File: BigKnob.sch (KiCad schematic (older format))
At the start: 10 parts, among them J1 NSJ12HF-1, J2 NSJ12HF-1, J3 NSJ12HF-1, J4 STEREO-JACK-SWITCHED-5-Pin, J5 STEREO-JACK-SWITCHED-5-Pin

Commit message: :punch: fixed schema
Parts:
- R1: renamed from R?; footprint (none) -> stahllabs:PTD904-1015F-A104
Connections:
- net CHASSIS_GND: now also R1.A3, R1.B3, R1.C3, R1.D3; no longer R1.A2, R1.B2, R1.C2, R1.D2
- net at J3.3 (RT): now also R1.B2; no longer R1.B3
- net at J3.5 (TT): now also R1.A2; no longer R1.A3
- net at J3.11 (TB): now also R1.C2; no longer R1.C3
- net at J3.9 (RB): now also R1.D2; no longer R1.D3
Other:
- moved on the sheet: J3A, J3B, R1A, R1B, R1C, R1D
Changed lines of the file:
@@
 $EndComp
 Wire Wire Line
-	3150 2700 3300 2700
-Wire Wire Line
-	3300 2700 3500 2700
-Wire Wire Line
-	3150 3600 3300 3600
-Wire Wire Line
-	3300 3600 3500 3600
-Wire Wire Line
-	3150 4750 3300 4750
-Wire Wire Line
-	3300 4750 3500 4750
+	3150 2700 3500 2700
+Wire Wire Line
+	3150 3600 3500 3600
+Wire Wire Line
+	3150 4750 3500 4750
 Text GLabel 3500 2700 2    60   Input ~ 0
 CHASSIS_GND
@@
 CHASSIS_GND
 Wire Wire Line
-	3150 5650 3300 5650
-Wire Wire Line
-	3300 5650 3500 5650
+	3150 5650 3500 5650
 Text GLabel 3500 5650 2    60   Input ~ 0
 CHASSIS_GND
@@
 L NSJ12HF-1 J3
 U 1 1 58E15C9F
-P 8350 3750
-F 0 "J3" H 8400 3350 60  0000 C CNN
-F 1 "NSJ12HF-1" H 8400 4050 60  0000 C CNN
-F 2 "stahllabs:NSJ12HF-1" H 8700 3900 60  0001 C CNN
-F 3 "http://www.neutrik.com/en/audio/plugs-and-jacks/stacking-jacks/nsj12hf-1" H 8400 3250 21  0001 C BIN
-	1    8350 3750
+P 8350 3700
+F 0 "J3" H 8400 3300 60  0000 C CNN
+F 1 "NSJ12HF-1" H 8400 4000 60  0000 C CNN
+F 2 "stahllabs:NSJ12HF-1" H 8700 3850 60  0001 C CNN
+F 3 "http://www.neutrik.com/en/audio/plugs-and-jacks/stacking-jacks/nsj12hf-1" H 8400 3200 21  0001 C BIN
+	1    8350 3700
 	-1   0    0    1
 $EndComp
@@
 L NSJ12HF-1 J3
 U 2 1 58E15D3A
-P 8350 4600
-F 0 "J3" H 8400 4200 60  0000 C CNN
-F 1 "NSJ12HF-1" H 8350 4900 60  0000 C CNN
-F 2 "stahllabs:NSJ12HF-1" H 8700 4750 60  0001 C CNN
-F 3 "http://www.neutrik.com/en/audio/plugs-and-jacks/stacking-jacks/nsj12hf-1" H 8400 4100 21  0001 C BIN
-	2    8350 4600
+P 8350 4700
+F 0 "J3" H 8400 4300 60  0000 C CNN
+F 1 "NSJ12HF-1" H 8350 5000 60  0000 C CNN
+F 2 "stahllabs:NSJ12HF-1" H 8700 4850 60  0001 C CNN
+F 3 "http://www.neutrik.com/en/audio/plugs-and-jacks/stacking-jacks/nsj12hf-1" H 8400 4200 21  0001 C BIN
+	2    8350 4700
 	-1   0    0    1
 $EndComp
 Wire Wire Line
-	7450 4050 7450 4500
-Wire Wire Line
-	7450 4500 7800 4500
-Wire Wire Line
-	7350 4300 7350 4650
-Wire Wire Line
-	7350 4650 7800 4650
+	6950 4250 6950 4600
+Wire Wire Line
+	6950 4600 7800 4600
+Wire Wire Line
+	6500 4750 7800 4750
 Wire Wire Line
 	3150 4550 4550 4550
 Wire Wire Line
-	4550 3600 4550 4550
-Wire Wire Line
-	4550 4550 4550 6500
-Wire Wire Line
-	6500 3550 7700 3550
-Wire Wire Line
-	7700 3550 7800 3650
-Text Notes 8950 3600 0    60   Italic 12
+	4550 3600 4550 6500
+Text Notes 8950 3550 0    60   Italic 12
 LEFT
 Text Notes 1800 2650 0    60   Italic 12
@@
 RIGHT
 Wire Wire Line
-	6500 3800 7800 3800
-Wire Wire Line
-	7550 4300 7800 4300
-Wire Wire Line
-	7550 3450 7550 3950
-Wire Wire Line
-	7550 3950 7550 4300
-Wire Wire Line
-	7550 4300 7550 4800
-Wire Wire Line
-	7800 3950 7550 3950
-Connection ~ 7550 3950
-Wire Wire Line
-	7550 4800 7800 4800
-Connection ~ 7550 4300
-Wire Wire Line
-	6500 4050 7450 4050
-Wire Wire Line
-	6500 4300 7350 4300
+	7650 4400 7800 4400
+Wire Wire Line
+	7650 3400 7650 4900
+Wire Wire Line
+	7800 3900 7650 3900
+Connection ~ 7650 3900
+Wire Wire Line
+	7650 4900 7800 4900
+Connection ~ 7650 4400
 Text Notes 8950 4450 0    60   Italic 12
 RIGHT
 Wire Wire Line
-	3150 2500 4450 2500
-Wire Wire Line
-	4450 2500 5000 2500
+	3150 2500 5000 2500
 Wire Wire Line
 	5000 2500 5000 3500
@@
 Connection ~ 3300 3600
 Wire Wire Line
-	7550 3450 7800 3450
-Text GLabel 7550 3450 0    60   Input ~ 0
-CHASSIS_GND
-Wire Wire Line
-	3150 3400 4550 3400
-Wire Wire Line
-	4550 3400 4800 3400
+	7650 3400 7800 3400
+Text GLabel 7650 3400 0    60   Input ~ 0
+CHASSIS_GND
+Wire Wire Line
+	3150 3400 4800 3400
 Wire Wire Line
 	4800 3400 4800 4000
@@
 	4800 4000 5000 4000
 Wire Wire Line
-	3150 5450 4450 5450
-Wire Wire Line
-	4450 5450 4800 5450
+	3150 5450 4800 5450
 Wire Wire Line
 	4800 5450 4800 4100
@@
 INPUT A\nmini jack
 Wire Wire Line
-	5550 3550 6100 3550
-Wire Wire Line
-	5550 3800 6100 3800
-Wire Wire Line
-	5550 4050 6100 4050
-Wire Wire Line
-	5550 4300 6100 4300
-Wire Wire Line
-	6300 3350 6600 3350
-Wire Wire Line
-	6600 3350 6600 3600
-Wire Wire Line
-	6600 3600 6600 3850
-Wire Wire Line
-	6600 3850 6600 4100
-Wire Wire Line
-	6600 4100 6600 4500
-Text GLabel 6600 4500 0    60   Input ~ 0
-CHASSIS_GND
-Wire Wire Line
-	6300 3600 6600 3600
-Connection ~ 6600 3600
-Wire Wire Line
-	6300 3850 6600 3850
-Wire Wire Line
-	6600 3850 6600 3850
-Connection ~ 6600 3850
-Wire Wire Line
-	6300 4100 6600 4100
-Connection ~ 6600 4100
-$Comp
-L PTD904-1015F-A104 R?
+	5550 4050 6300 4050
+Text GLabel 6100 5100 2    60   Input ~ 0
+CHASSIS_GND
+$Comp
+L PTD904-1015F-A104 R1
 U 1 1 58FEAB86
-P 6300 3550
-F 0 "R?" H 6300 3800 20  0000 C CNN
-F 1 "PTD904-1015F-A104" H 6300 3475 20  0000 C CNN
-F 2 "" H 6300 3550 60  0001 C CNN
-F 3 "" H 6300 3550 60  0001 C CNN
-	1    6300 3550
-	1    0    0    -1
-$EndComp
-$Comp
-L PTD904-1015F-A104 R?
+P 6300 3250
+F 0 "R1" H 6300 3500 20  0000 C CNN
+F 1 "PTD904-1015F-A104" H 6300 3175 20  0000 C CNN
+F 2 "stahllabs:PTD904-1015F-A104" H 6300 3250 60  0001 C CNN
+F 3 "" H 6300 3250 60  0001 C CNN
+	1    6300 3250
+	0    1    1    0
+$EndComp
+$Comp
+L PTD904-1015F-A104 R1
 U 2 1 58FEABBF
-P 6300 3800
-F 0 "R?" H 6300 4050 20  0000 C CNN
-F 1 "PTD904-1015F-A104" H 6300 3725 20  0000 C CNN
-F 2 "" H 6300 3800 60  0001 C CNN
-F 3 "" H 6300 3800 60  0001 C CNN
-	2    6300 3800
-	1    0    0    -1
-$EndComp
-$Comp
-L PTD904-1015F-A104 R?
-U 3 1 58FEAC45
-P 6300 4050
-F 0 "R?" H 6300 4300 20  0000 C CNN
-F 1 "PTD904-1015F-A104" H 6300 3975 20  0000 C CNN
-F 2 "" H 6300 4050 60  0001 C CNN
-F 3 "" H 6300 4050 60  0001 C CNN
-	3    6300 4050
-	1    0    0    -1
-$EndComp
-$Comp
-L PTD904-1015F-A104 R?
+P 6300 3750
+F 0 "R1" H 6300 4000 20  0000 C CNN
+F 1 "PTD904-1015F-A104" H 6300 3675 20  0000 C CNN
+F 2 "stahllabs:PTD904-1015F-A104" H 6300 3750 60  0001 C CNN
+F 3 "" H 6300 3750 60  0001 C CNN
+	2    6300 3750
+	0    1    1    0
+$EndComp
+$Comp
+L PTD904-1015F-A104 R1
 U 4 1 58FEAC80
-P 6300 4300
-F 0 "R?" H 6300 4550 20  0000 C CNN
-F 1 "PTD904-1015F-A104" H 6300 4225 20  0000 C CNN
-F 2 "" H 6300 4300 60  0001 C CNN
-F 3 "" H 6300 4300 60  0001 C CNN
-	4    6300 4300
-	1    0    0    -1
+P 6300 4750
+F 0 "R1" H 6300 5000 20  0000 C CNN
+F 1 "PTD904-1015F-A104" H 6300 4675 20  0000 C CNN
+F 2 "stahllabs:PTD904-1015F-A104" H 6300 4750 60  0001 C CNN
+F 3 "" H 6300 4750 60  0001 C CNN
+	4    6300 4750
+	0    1    1    0
 $EndComp
 Wire Notes Line
@@
 SWITCH
 Wire Notes Line
-	5900 4600 6700 4600
-Wire Notes Line
-	6700 4600 6700 3100
-Wire Notes Line
-	6700 3100 5900 3100
-Wire Notes Line
-	5900 3100 5900 4600
-Text Notes 6000 3250 0    99   Italic 20
+	5900 2700 6800 2700
+Wire Notes Line
+	5900 2700 5900 5250
+Text Notes 6000 2900 0    99   Italic 20
 VOLUME
+Wire Wire Line
+	6600 3250 6600 3600
+Wire Wire Line
+	6600 3600 7800 3600
+Wire Wire Line
+	6500 3750 7800 3750
+$Comp
+L PTD904-1015F-A104 R1
+U 3 1 58FEAC45
+P 6300 4250
+F 0 "R1" H 6300 4500 20  0000 C CNN
+F 1 "PTD904-1015F-A104" H 6300 4175 20  0000 C CNN
+F 2 "stahllabs:PTD904-1015F-A104" H 6300 4250 60  0001 C CNN
+F 3 "" H 6300 4250 60  0001 C CNN
+	3    6300 4250
+	0    1    1    0
+$EndComp
+Wire Wire Line
+	5550 3550 6000 3550
+Wire Wire Line
+	6000 3550 6000 3050
+Wire Wire Line
+	6000 3050 6300 3050
+Wire Wire Line
+	6500 3250 6600 3250
+Wire Wire Line
+	5550 4300 6200 4300
+Wire Wire Line
+	6200 4300 6200 4550
+Wire Wire Line
+	6200 4550 6300 4550
+Wire Wire Line
+	5550 3800 6200 3800
+Wire Wire Line
+	6200 3800 6200 3550
+Wire Wire Line
+	6200 3550 6300 3550
+Wire Notes Line
+	6800 2700 6800 5250
+Wire Wire Line
+	7450 3750 7450 3750
+Wire Wire Line
+	6950 4250 6500 4250
+Wire Wire Line
+	6100 3450 6100 5100
+Wire Wire Line
+	6100 3450 6300 3450
+Wire Wire Line
+	6300 3950 6100 3950
+Connection ~ 6100 3950
+Wire Wire Line
+	6300 4450 6100 4450
+Connection ~ 6100 4450
+Wire Wire Line
+	6300 4950 6100 4950
+Connection ~ 6100 4950
+Wire Notes Line
+	6800 5250 5900 5250
 $EndSCHEMATC

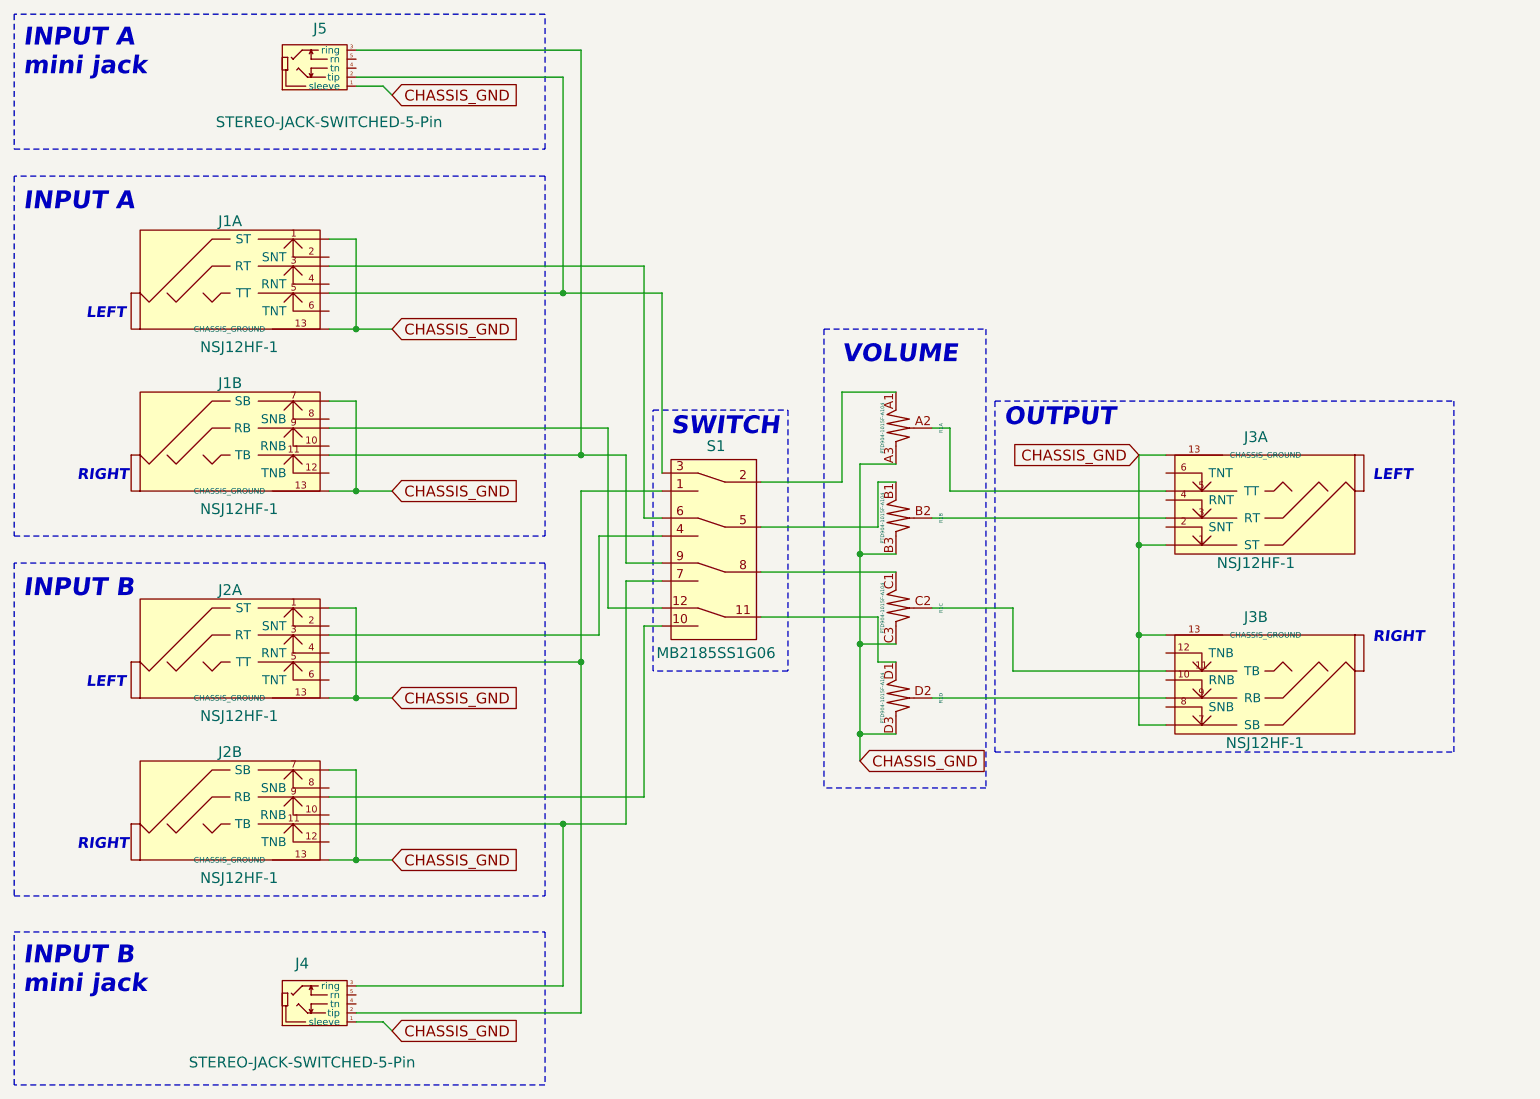
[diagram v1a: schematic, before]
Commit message: fix library paths
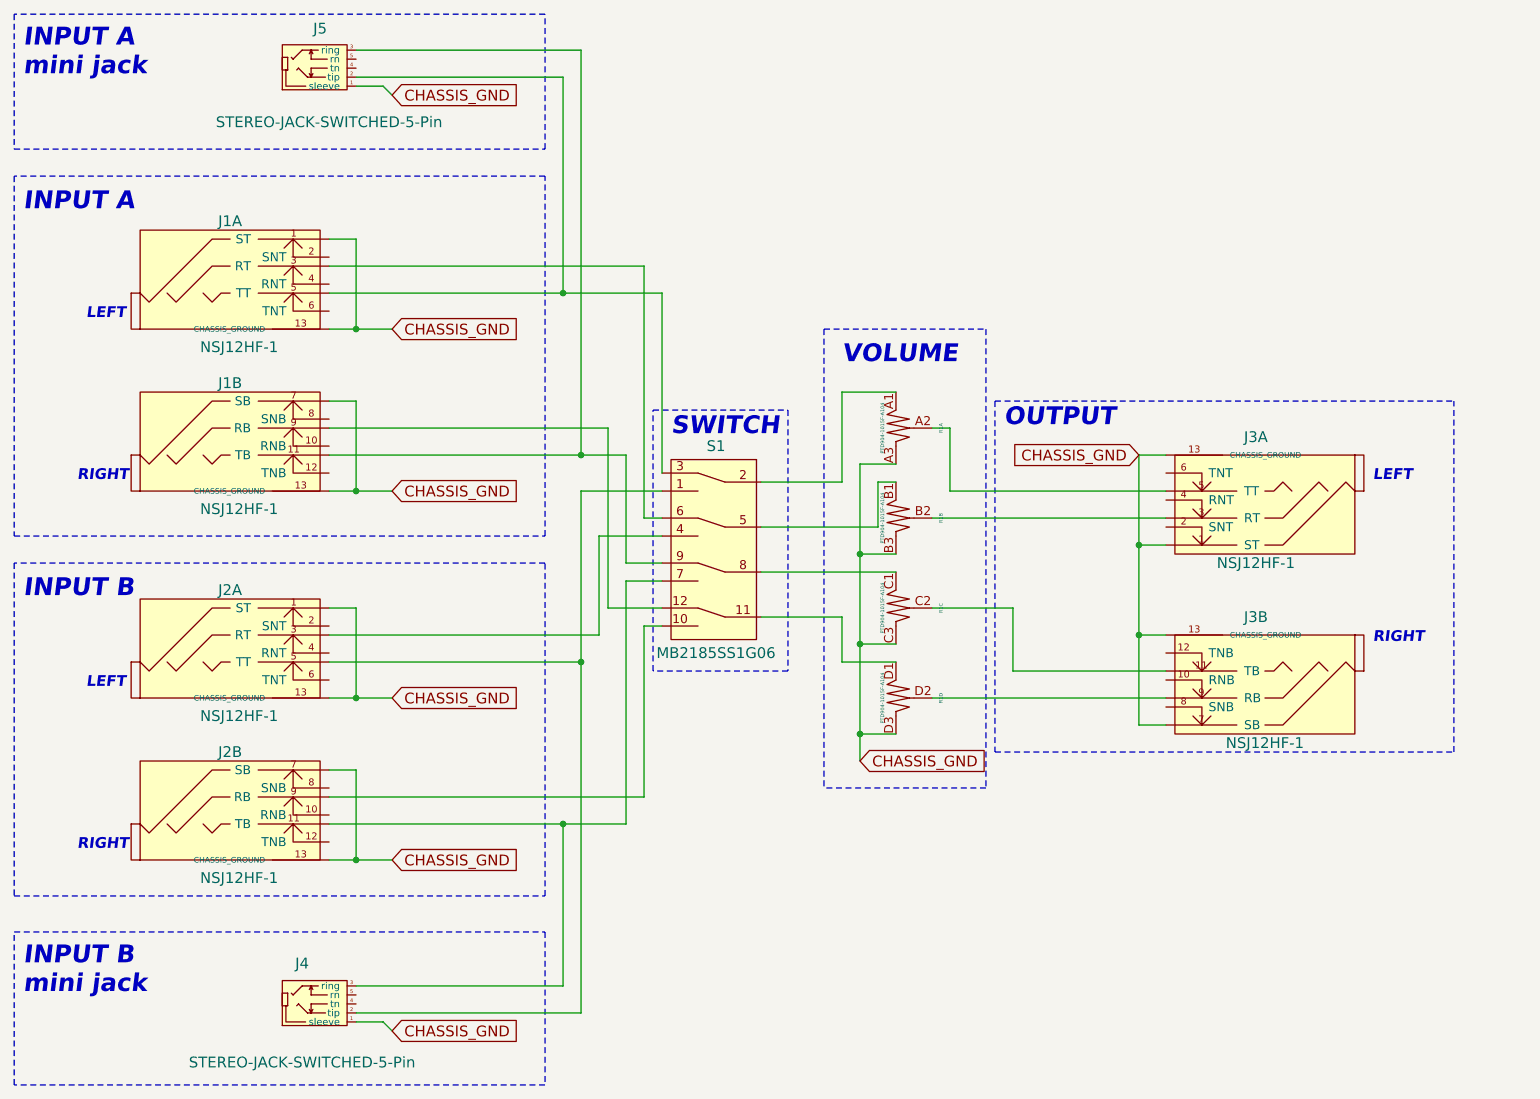
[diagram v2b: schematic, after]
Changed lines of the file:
@@
 $EndComp
 Wire Wire Line
-	3150 2700 3500 2700
-Wire Wire Line
-	3150 3600 3500 3600
-Wire Wire Line
-	3150 4750 3500 4750
+	3150 2700 3300 2700
+Wire Wire Line
+	3300 2700 3500 2700
+Wire Wire Line
+	3150 3600 3300 3600
+Wire Wire Line
+	3300 3600 3500 3600
+Wire Wire Line
+	3150 4750 3300 4750
+Wire Wire Line
+	3300 4750 3500 4750
 Text GLabel 3500 2700 2    60   Input ~ 0
 CHASSIS_GND
@@
 CHASSIS_GND
 Wire Wire Line
-	3150 5650 3500 5650
+	3150 5650 3300 5650
+Wire Wire Line
+	3300 5650 3500 5650
 Text GLabel 3500 5650 2    60   Input ~ 0
 CHASSIS_GND
@@
 	3150 4550 4550 4550
 Wire Wire Line
-	4550 3600 4550 6500
+	4550 3600 4550 4550
+Wire Wire Line
+	4550 4550 4550 6500
 Text Notes 8950 3550 0    60   Italic 12
 LEFT
@@
 	7650 4400 7800 4400
 Wire Wire Line
-	7650 3400 7650 4900
+	7650 3400 7650 3900
+Wire Wire Line
+	7650 3900 7650 4400
+Wire Wire Line
+	7650 4400 7650 4900
 Wire Wire Line
 	7800 3900 7650 3900
@@
 RIGHT
 Wire Wire Line
-	3150 2500 5000 2500
+	3150 2500 4450 2500
+Wire Wire Line
+	4450 2500 5000 2500
 Wire Wire Line
 	5000 2500 5000 3500
@@
 CHASSIS_GND
 Wire Wire Line
-	3150 3400 4800 3400
+	3150 3400 4550 3400
+Wire Wire Line
+	4550 3400 4800 3400
 Wire Wire Line
 	4800 3400 4800 4000
@@
 	4800 4000 5000 4000
 Wire Wire Line
-	3150 5450 4800 5450
+	3150 5450 4450 5450
+Wire Wire Line
+	4450 5450 4800 5450
 Wire Wire Line
 	4800 5450 4800 4100
@@
 	6500 3250 6600 3250
 Wire Wire Line
-	5550 4300 6200 4300
-Wire Wire Line
-	6200 4300 6200 4550
-Wire Wire Line
-	6200 4550 6300 4550
+	5550 4300 6000 4300
+Wire Wire Line
+	6000 4300 6000 4550
+Wire Wire Line
+	6000 4550 6300 4550
 Wire Wire Line
 	5550 3800 6200 3800
@@
 	6950 4250 6500 4250
 Wire Wire Line
-	6100 3450 6100 5100
+	6100 3450 6100 3950
+Wire Wire Line
+	6100 3950 6100 4450
+Wire Wire Line
+	6100 4450 6100 4950
+Wire Wire Line
+	6100 4950 6100 5100
 Wire Wire Line
 	6100 3450 6300 3450
